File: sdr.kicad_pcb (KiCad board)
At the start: 4 copper layers, 65 x 56 mm, 224 parts, among them J1 RX, J2 TX, SW1 KMR231NGLFS, T1 B0322J5050, T2 B0322J5050, T3 TR_TC1-1-43X+, T4 TR_TC1-1-43X+, U1 FT601, U10 MIC94310, U11 PAM2305, U12 BGS12, U13 BGS12, U14 FT232HL, U15 93LCxxBT-I/OT, U3 LMS6002DR2, U4 ECP5, U5 Si5351, U6 PAM2305, U7 LD39200, U8 MIC94310, U9 MIC94310, X1 GSB443133HR, X2 JTAG, X3 RaspberryPiConnector, X4 JTAG, X5 USB_OTG, Y1 FL3000027, Y2 ABM11-141, Y3 ABLS2-12.000MHZ-D4Y-T

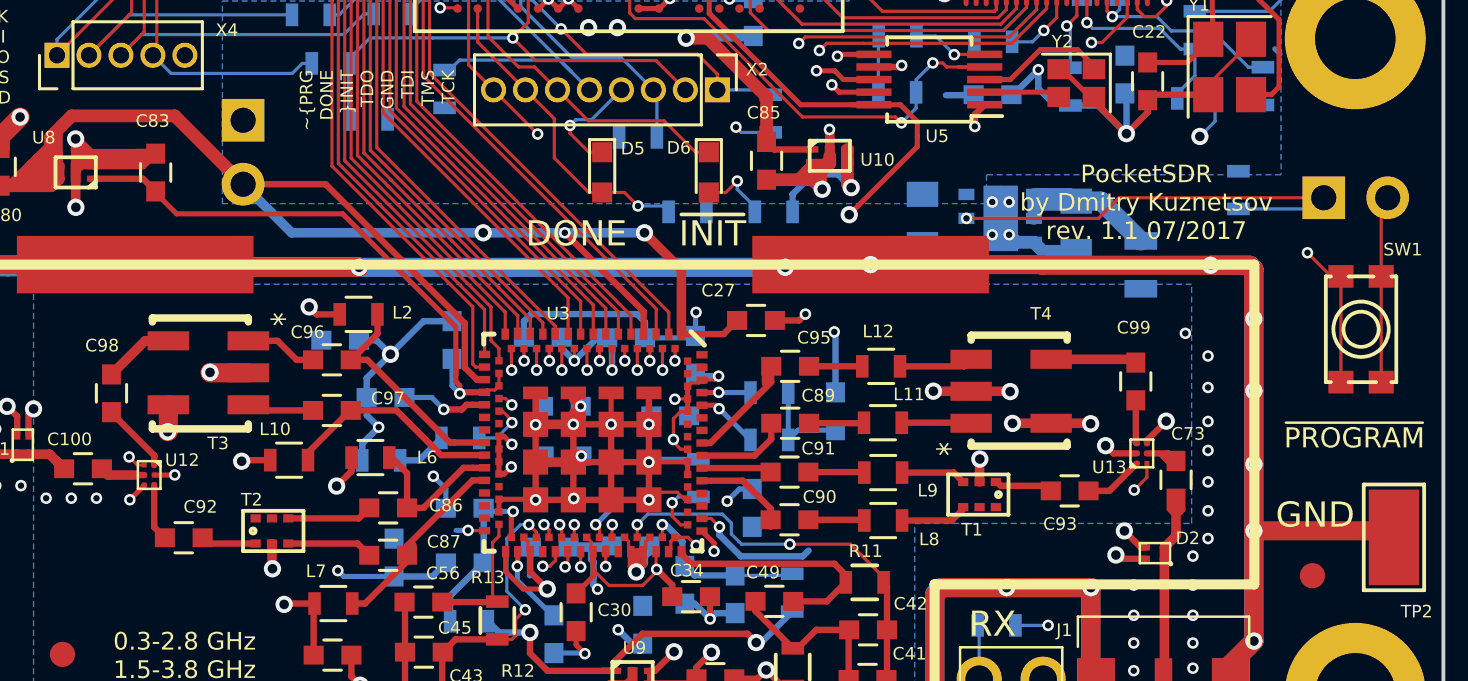
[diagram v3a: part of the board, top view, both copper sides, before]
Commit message: Fix silkscreen of update components. Fix width of fan outs of RF muxers to better soldering.
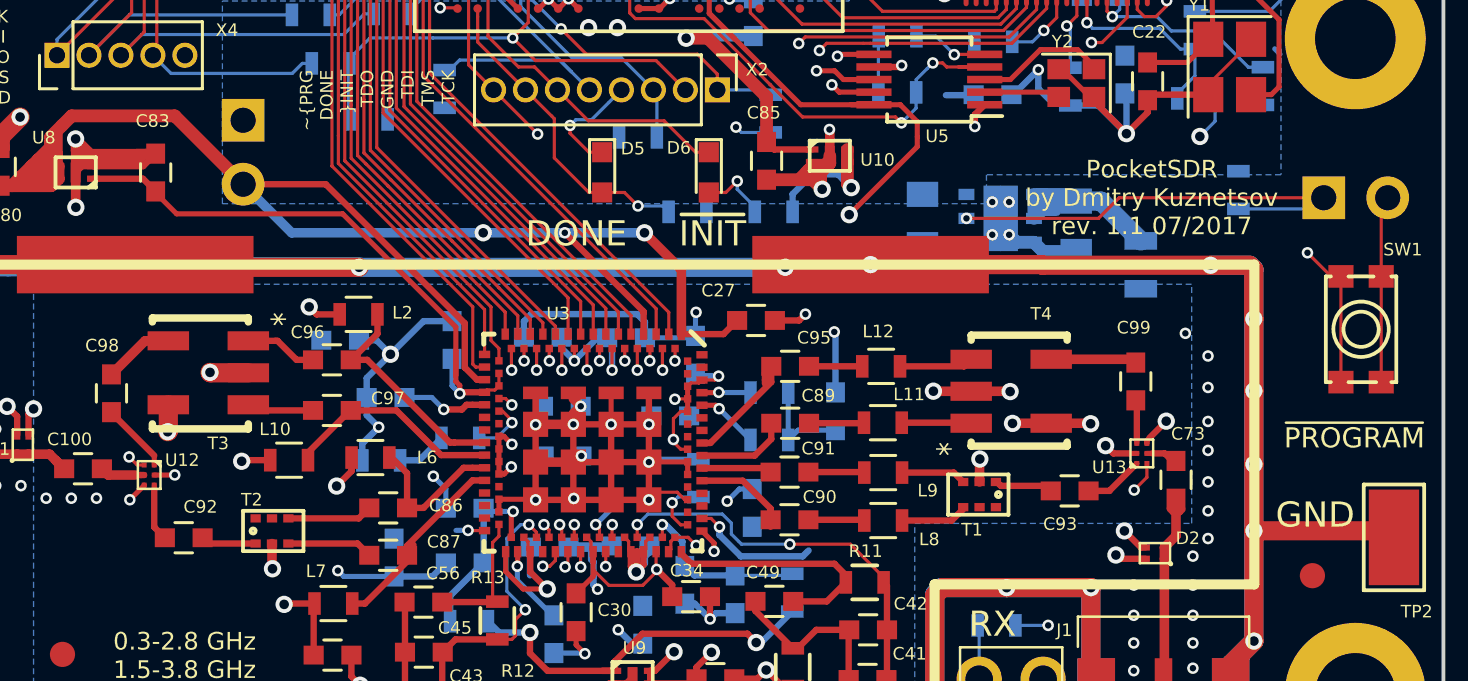
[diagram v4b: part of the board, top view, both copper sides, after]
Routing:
- net Net-(C79-Pad1): track 7.65 -> 8.66 mm
- net Net-(C73-Pad1): track 1.90 -> 1.28 mm
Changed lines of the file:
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@@
     (thickness 1.6)
     (drawings 25)
-    (tracks 3888)
+    (tracks 3900)
     (zones 0)
     (modules 224)
@@
     (0 F.Cu signal)
     (1 In1.Cu power hide)
-    (2 In2.Cu signal hide)
+    (2 In2.Cu signal)
     (31 B.Cu signal)
     (32 B.Adhes user hide)
@@
     (34 B.Paste user hide)
     (35 F.Paste user hide)
-    (36 B.SilkS user hide)
-    (37 F.SilkS user hide)
-    (38 B.Mask user)
+    (36 B.SilkS user)
+    (37 F.SilkS user)
+    (38 B.Mask user hide)
     (39 F.Mask user hide)
     (40 Dwgs.User user hide)
@@
   )
   (setup
-    (last_trace_width 0.762)
+    (last_trace_width 0.381)
     (user_trace_width 0.2032)
     (user_trace_width 0.254)
@@
     (tags "capacitor 0805")
     (attr smd)
-    (fp_text reference C79 (at 0 1.5 270) (layer B.SilkS)
-      (effects (font (size 1 1) (thickness 0.15)) (justify mirror))
+    (fp_text reference C79 (at -2.39268 0.10668 360) (layer B.SilkS)
+      (effects (font (size 0.5 0.5) (thickness 0.1)) (justify mirror))
     )
     (fp_text value 10u (at 0 -1.75 270) (layer B.Fab)
@@
     (tags "DFN 0.95")
     (attr smd)
-    (fp_text reference U7 (at 0 2.575 180) (layer B.SilkS)
-      (effects (font (size 1 1) (thickness 0.15)) (justify mirror))
+    (fp_text reference U7 (at -0.27768 2.2883 180) (layer B.SilkS)
+      (effects (font (size 0.5 0.5) (thickness 0.1)) (justify mirror))
     )
     (fp_text value LD39200 (at 0 -2.575 180) (layer B.Fab)
@@
     (tags "capacitor 0805")
     (attr smd)
-    (fp_text reference C78 (at 0 1.5 270) (layer B.SilkS)
-      (effects (font (size 1 1) (thickness 0.15)) (justify mirror))
+    (fp_text reference C78 (at -2.26314 0.09906 360) (layer B.SilkS)
+      (effects (font (size 0.5 0.5) (thickness 0.1)) (justify mirror))
     )
     (fp_text value 10u (at 0 -1.75 270) (layer B.Fab)
@@
     (effects (font (size 0.7 0.7) (thickness 0.1)))
   )
-  (gr_text "PocketSDR\nby Dmitry Kuznetsov\nrev. 1.1 07/2017" (at 153.2 133) (layer F.SilkS)
+  (gr_text "PocketSDR\nby Dmitry Kuznetsov\nrev. 1.1 07/2017" (at 153.41346 132.81152) (layer F.SilkS)
     (effects (font (size 0.7 0.7) (thickness 0.1)))
   )
@@
   (gr_line (start 158.1 106.4) (end 158.1 111.4) (angle 90) (layer F.CrtYd) (width 0.2))
   (segment (start 158.508601 127.108601) (end 158.3 126.9) (width 0.2032) (layer B.Cu) (net 0))
+  (segment (start 152.52192 142.96898) (end 151.88946 142.96898) (width 0.254) (layer F.Cu) (net 3))
+  (segment (start 152.6286 142.96898) (end 152.52192 142.96898) (width 0.2032) (layer F.Cu) (net 3))
+  (segment (start 152.82164 142.96898) (end 152.6286 142.96898) (width 0.2032) (layer F.Cu) (net 3))
   (segment (start 138.85672 135.57758) (end 142.14094 135.57758) (width 0.762) (layer B.Cu) (net 3))
   (segment (start 142.14094 135.57758) (end 142.24762 135.4709) (width 0.762) (layer B.Cu) (net 3))
@@
   (segment (start 148.73538 134.58424) (end 148.05 134.58424) (width 0.508) (layer B.Cu) (net 3))
   (segment (start 148.05 134.58424) (end 147.75 134.28424) (width 0.508) (layer B.Cu) (net 3))
-  (segment (start 152.82164 142.96898) (end 151.88946 142.96898) (width 0.254) (layer F.Cu) (net 3))
   (segment (start 151.88946 142.96898) (end 151.58212 142.66164) (width 0.254) (layer F.Cu) (net 3))
   (segment (start 138.85672 135.57758) (end 121.93016 135.57758) (width 0.762) (layer B.Cu) (net 3))
@@
   (segment (start 132.09224 151.60536) (end 131.58824 151.60536) (width 0.254) (layer F.Cu) (net 60))
   (via (at 128.71704 150.08352) (size 0.6858) (drill 0.381) (layers F.Cu B.Cu) (net 60))
-  (segment (start 153.22164 142.56898) (end 153.22164 142.45722) (width 0.254) (layer F.Cu) (net 61))
-  (segment (start 153.22164 142.45722) (end 153.99004 141.68882) (width 0.254) (layer F.Cu) (net 61))
+  (segment (start 153.32456 142.3543) (end 153.22164 142.45722) (width 0.2032) (layer F.Cu) (net 61))
+  (segment (start 153.22164 142.45722) (end 153.22164 142.56898) (width 0.2032) (layer F.Cu) (net 61))
+  (segment (start 153.32456 142.3543) (end 153.99004 141.68882) (width 0.254) (layer F.Cu) (net 61))
+  (segment (start 153.22164 142.56898) (end 153.22164 142.56644) (width 0.2032) (layer F.Cu) (net 61))
   (segment (start 139.552679 147.058381) (end 139.78382 146.82724) (width 0.254) (layer B.Cu) (net 61))
   (segment (start 136.2456 145.88744) (end 136.2456 146.210729) (width 0.254) (layer B.Cu) (net 61))
@@
   (via (at 139.05 114.52) (size 0.4572) (drill 0.254) (layers F.Cu B.Cu) (net 188))
   (segment (start 138.64 114.1) (end 138.64 114.11) (width 0.127) (layer F.Cu) (net 188))
+  (segment (start 149.10962 133.35) (end 149.62632 133.35) (width 0.381) (layer B.Cu) (net 191))
+  (segment (start 148.73538 133.63424) (end 148.82538 133.63424) (width 0.381) (layer B.Cu) (net 191))
+  (segment (start 148.82538 133.63424) (end 149.10962 133.35) (width 0.381) (layer B.Cu) (net 191))
   (segment (start 149.02434 132.95182) (end 149.02672 132.94944) (width 0.762) (layer B.Cu) (net 191))
   (segment (start 150.41372 132.94944) (end 149.02672 132.94944) (width 0.762) (layer B.Cu) (net 191))
@@
   (segment (start 117.82092 146.54962) (end 115.94586 146.54962) (width 0.254) (layer F.Cu) (net 201))
   (segment (start 115.94586 146.54962) (end 115.71548 146.31924) (width 0.254) (layer F.Cu) (net 201))
-  (segment (start 113.79454 144.22872) (end 113.79454 145.8983) (width 0.254) (layer F.Cu) (net 202))
+  (segment (start 113.79454 144.44218) (end 113.79454 145.8983) (width 0.254) (layer F.Cu) (net 202))
+  (segment (start 113.79454 144.22872) (end 113.79454 144.44218) (width 0.2032) (layer F.Cu) (net 202))
   (segment (start 113.79454 145.8983) (end 114.21548 146.31924) (width 0.254) (layer F.Cu) (net 202))
   (segment (start 147.22578 144.10436) (end 147.26578 144.10436) (width 0.254) (layer F.Cu) (net 203))
@@
   (segment (start 147.41818 144.25676) (end 149.20398 144.25676) (width 0.254) (layer F.Cu) (net 203))
   (segment (start 149.20398 144.25676) (end 149.40464 144.45742) (width 0.254) (layer F.Cu) (net 203))
+  (segment (start 152.69464 143.49476) (end 151.7332 144.4562) (width 0.254) (layer F.Cu) (net 204))
+  (segment (start 151.7332 144.4562) (end 151.7332 144.45742) (width 0.254) (layer F.Cu) (net 204))
+  (segment (start 152.82042 143.36898) (end 152.69464 143.49476) (width 0.2032) (layer F.Cu) (net 204))
+  (segment (start 152.82164 143.36898) (end 152.82042 143.36898) (width 0.2032) (layer F.Cu) (net 204))
   (segment (start 150.90464 144.45742) (end 151.7332 144.45742) (width 0.254) (layer F.Cu) (net 204))
-  (segment (start 151.7332 144.45742) (end 152.82164 143.36898) (width 0.254) (layer F.Cu) (net 204))
   (segment (start 140.85316 142.04512) (end 139.36726 142.04512) (width 0.2032) (layer B.Cu) (net 205))
   (segment (start 139.36726 142.04512) (end 138.9768 142.43558) (width 0.2032) (layer B.Cu) (net 205))
@@
   (segment (start 125.18898 143.03756) (end 123.41352 141.2621) (width 0.254) (layer F.Cu) (net 215))
   (segment (start 123.41352 141.2621) (end 121.60066 141.2621) (width 0.254) (layer F.Cu) (net 215))
+  (segment (start 113.79454 143.42872) (end 113.79454 143.05564) (width 0.2032) (layer F.Cu) (net 216))
   (segment (start 112.09528 141.33138) (end 112.09528 141.35638) (width 0.254) (layer F.Cu) (net 216))
   (segment (start 112.09528 141.35638) (end 113.79454 143.05564) (width 0.254) (layer F.Cu) (net 216))
-  (segment (start 113.79454 143.05564) (end 113.79454 143.07472) (width 0.254) (layer F.Cu) (net 216))
-  (segment (start 113.79454 143.07472) (end 113.79454 143.42872) (width 0.254) (layer F.Cu) (net 216))
   (segment (start 114.35354 138.49746) (end 113.4292 138.49746) (width 0.381) (layer F.Cu) (net 217))
   (segment (start 113.4292 138.49746) (end 112.09528 139.83138) (width 0.381) (layer F.Cu) (net 217))
@@
   (segment (start 102.22176 143) (end 102.20706 143.0147) (width 0.381) (layer F.Cu) (net 219))
   (segment (start 109.8804 143.244) (end 110.21498 143.57858) (width 0.381) (layer F.Cu) (net 219))
-  (segment (start 153.22164 142.96898) (end 154.07964 142.96898) (width 0.254) (layer F.Cu) (net 220))
-  (segment (start 154.07964 142.96898) (end 154.37866 143.268) (width 0.254) (layer F.Cu) (net 220))
-  (segment (start 154.05792 143.268) (end 153.8478 143.05788) (width 0.254) (layer F.Cu) (net 220))
-  (segment (start 154.37866 143.268) (end 154.05792 143.268) (width 0.254) (layer F.Cu) (net 220))
+  (segment (start 153.92908 142.96898) (end 154.2281 143.268) (width 0.254) (layer F.Cu) (net 220))
+  (segment (start 154.2281 143.268) (end 154.37866 143.268) (width 0.254) (layer F.Cu) (net 220))
+  (segment (start 153.43632 142.96898) (end 153.92908 142.96898) (width 0.254) (layer F.Cu) (net 220))
+  (segment (start 153.34996 142.96898) (end 153.43632 142.96898) (width 0.2032) (layer F.Cu) (net 220))
+  (segment (start 153.22164 142.96898) (end 153.34996 142.96898) (width 0.2032) (layer F.Cu) (net 220))
   (segment (start 153.91638 147.1549) (end 153.91638 153.41854) (width 0.381) (layer F.Cu) (net 221))
   (segment (start 153.91638 153.41854) (end 153.88082 153.4541) (width 0.381) (layer F.Cu) (net 221))
@@
   (segment (start 149.42038 139.23122) (end 152.65074 139.23122) (width 0.381) (layer F.Cu) (net 225))
   (segment (start 152.65074 139.23122) (end 152.781 139.36148) (width 0.381) (layer F.Cu) (net 225))
-  (segment (start 152.781 140.86148) (end 152.781 142.52834) (width 0.254) (layer F.Cu) (net 226))
-  (segment (start 152.781 142.52834) (end 152.82164 142.56898) (width 0.254) (layer F.Cu) (net 226))
+  (segment (start 152.82164 142.42542) (end 152.82164 140.90212) (width 0.254) (layer F.Cu) (net 226))
+  (segment (start 152.82164 140.90212) (end 152.781 140.86148) (width 0.254) (layer F.Cu) (net 226))
+  (segment (start 152.82164 142.56898) (end 152.82164 142.42542) (width 0.2032) (layer F.Cu) (net 226))
   (segment (start 143.4853 141.74978) (end 146.2214 141.74978) (width 0.254) (layer F.Cu) (net 227))
   (segment (start 146.2214 141.74978) (end 146.24284 141.77122) (width 0.254) (layer F.Cu) (net 227))

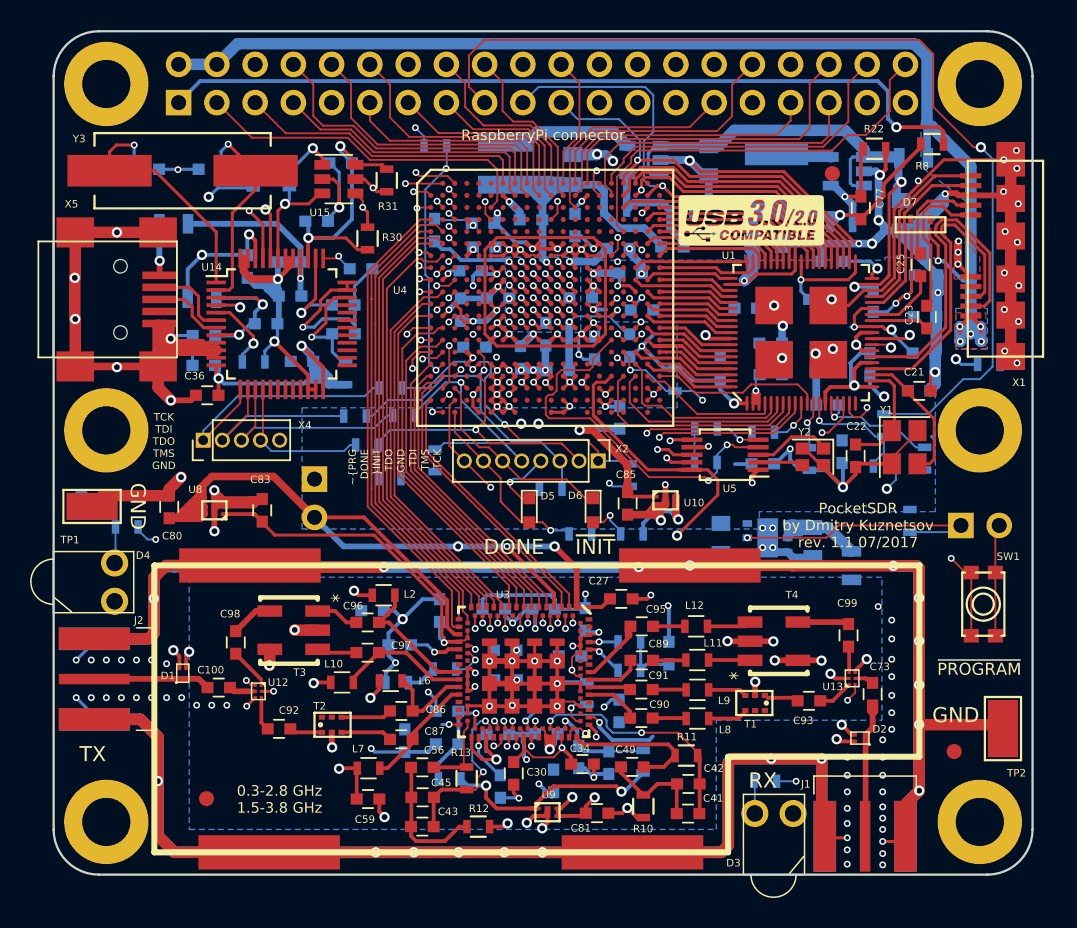
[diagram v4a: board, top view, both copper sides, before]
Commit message: Change footprints for LMS and FT601 to allow mask resist between pads. Now only ESD7016 and RF muxers have no mask due to very low pitch.
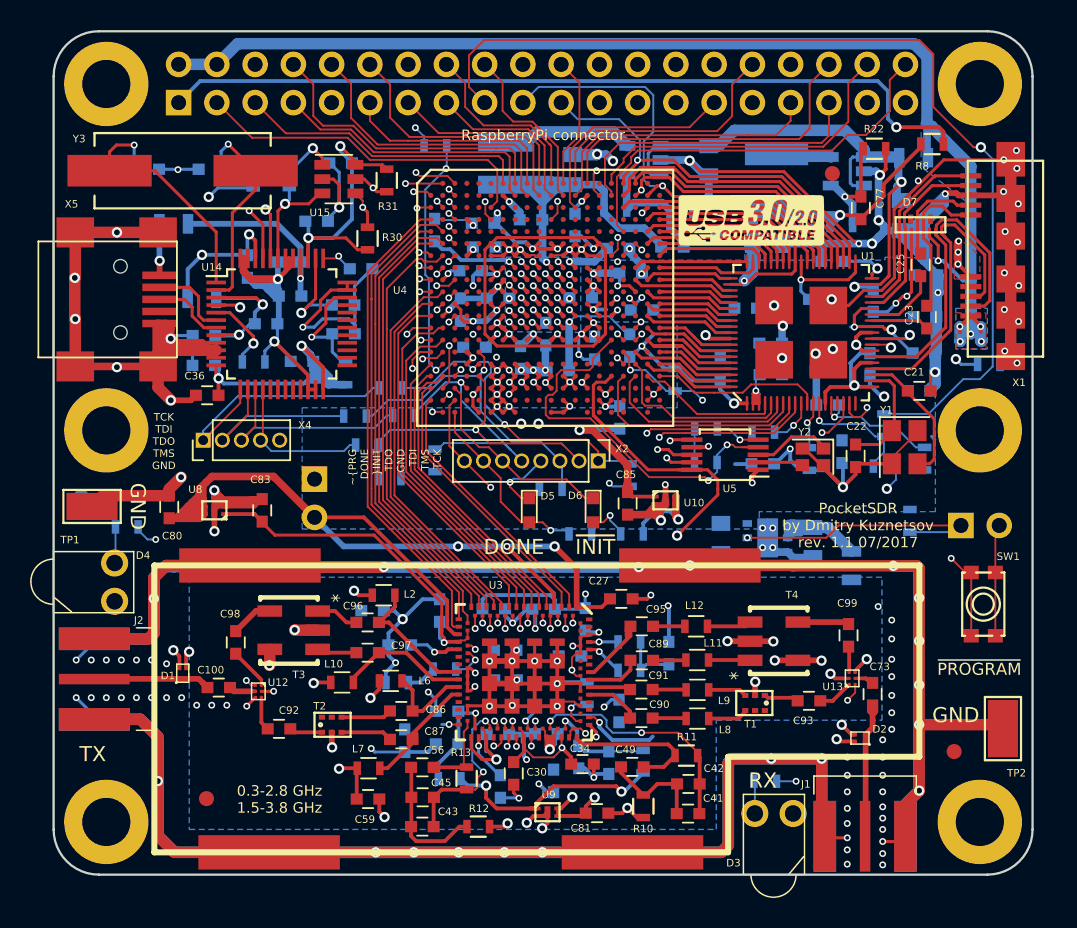
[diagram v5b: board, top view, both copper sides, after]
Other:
- rule pad_to_mask_clearance: 0.07112 -> 0.0635
- rule solder_mask_min_width: 0.127 -> 0.1016
